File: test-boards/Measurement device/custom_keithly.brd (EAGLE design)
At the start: 160 x 100 mm, 49 parts, among them IC1 TL071D, IC2 7805L, IC3 7905L, U1 AD8220, U2 INA333, U3 INA333

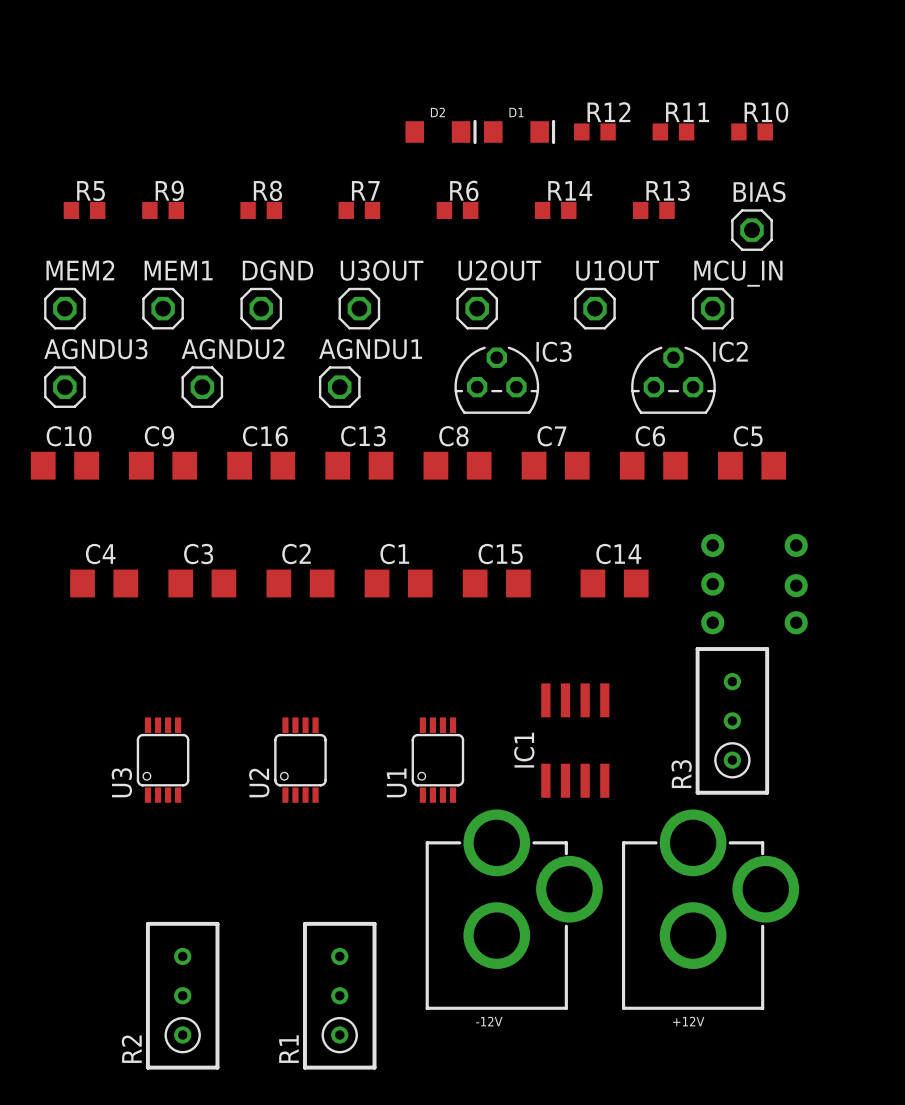
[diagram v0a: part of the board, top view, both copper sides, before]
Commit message: added doc for required .lbr files and basic BOM
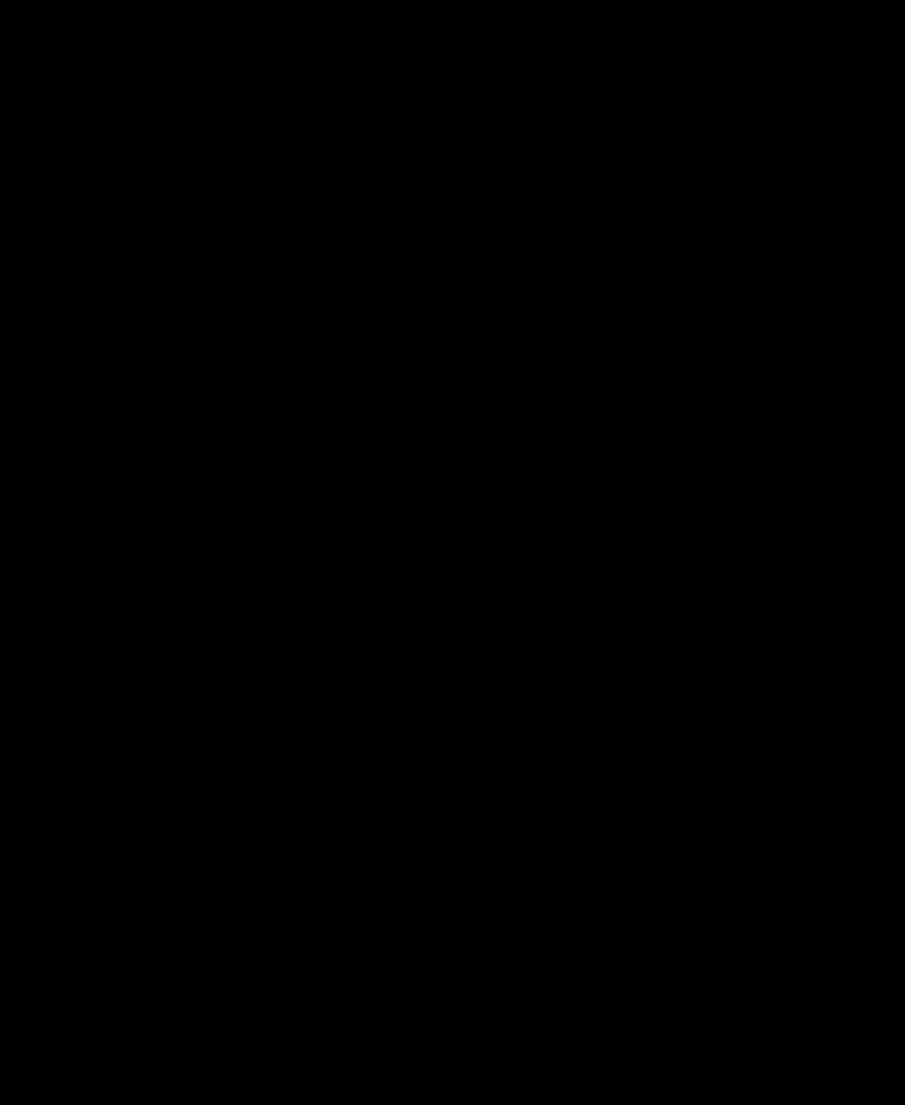
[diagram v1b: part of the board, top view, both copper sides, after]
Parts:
- removed +12V, -12V: POWER_JACK, SparkFun-Connectors:POWER_JACK_PTH
- removed AGNDU1, AGNDU2, AGNDU3, BIAS, DGND, MCU_IN, MEM1, MEM2, U1OUT, U2OUT, U3OUT: (no value), pinhead:1X01
- removed C1, C13, C16, C2, C3, C4, C5, C6, C7, C8: 0.1uF, rcl:C3216
- removed C10, C9: 10uF, rcl:C3216
- removed C14, C15: 0.33uF, rcl:C3216
- removed D1: RED, SparkFun-LED:LED-1206
- removed D2: YELLOW, SparkFun-LED:LED-1206
- removed IC1: TL071D, linear:SO08
- removed IC2: 7805L, linear:TO92
- removed IC3: 7905L, linear:TO92
- removed R1, R2, R3: 100R, rcl:RTRIM3296W
- removed R10, R11, R12: 30R, rcl:R0603
- removed R13, R14: 220R, rcl:R0603
- removed R5: 10R, rcl:R0603
- removed R6, R7, R8, R9: 100K, rcl:R0603
- removed U$1: PS850L_BUTTON, untitled:PS850L
- removed U1: AD8220, untitled:MSOP08
- removed U2, U3: INA333, untitled:MSOP08
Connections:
- removed net +5V: C1.1, C3.1, C5.1, C7.1, C9.1, D1.C, IC1.7, U$1.P$6, U1.8, U2.7, U3.7
- removed net -5V: C10.1, C2.2, C4.2, C6.2, C8.1, D2.A, IC1.4, U$1.P$3, U1.5, U2.4, U3.4
- removed net AGND: +12V.GNDBREAK, -12V.GNDBREAK, AGNDU1.1, AGNDU2.1, AGNDU3.1, C1.2, C10.2, C2.1, C3.2, C4.1, C5.2, C6.1, C7.2, C8.2, C9.2, MEM2.1, U1.6, U2.3, U2.5, U3.3, U3.5
- removed net GND: +12V.GND, -12V.GND, C13.1, C14.1, C15.2, C16.2, DGND.1, IC2.2, IC3.1, R13.1, R14.1, R9.2
- removed net IN+: IC1.6, R5.1, R7.2, U1.4
- removed net IN-: MEM1.1, R5.2, U1.1
- removed net MCU_IN: MCU_IN.1, R8.1
- removed net N$1: IC1.2, R6.2, R7.1
- removed net N$10: -12V.PWR, C15.1, IC3.2
- removed net N$11: C13.2, IC2.1, U$1.P$5
- removed net N$15: C16.1, IC3.3, U$1.P$2
- removed net N$2: IC1.3, R8.2, R9.1
- removed net N$3: R1.1, R10.1
- removed net N$4: R11.1, R2.3
- removed net N$5: R12.1, R3.3
- removed net N$7: +12V.PWR, C14.2, IC2.3
- removed net N$8: D1.A, R13.2
- removed net N$9: D2.C, R14.2
- removed net U1OUT: U1.7, U1OUT.1, U2.2
- removed net U1RG1: R1.2, U1.3
- removed net U1RG2: R10.2, U1.2
- removed net U2OUT: U2.6, U2OUT.1, U3.2
- removed net U2RG1: R11.2, U2.1
- removed net U2RG2: R2.2, U2.8
- removed net U3OUT: U3.6, U3OUT.1
- removed net U3RG1: R12.2, U3.1
- removed net U3RG2: R3.2, U3.8
- removed net V+: BIAS.1, R6.1

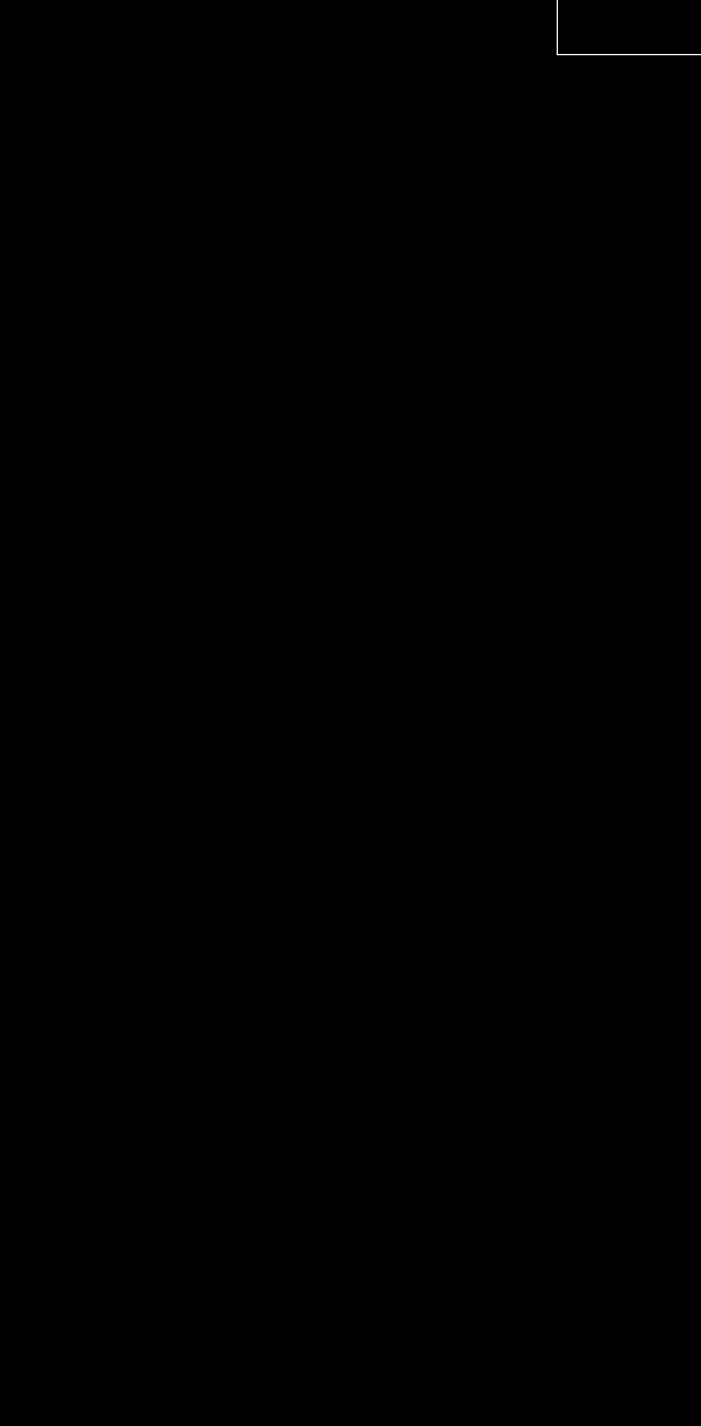
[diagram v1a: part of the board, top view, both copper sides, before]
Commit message: created part of the schematic and added some datasheets
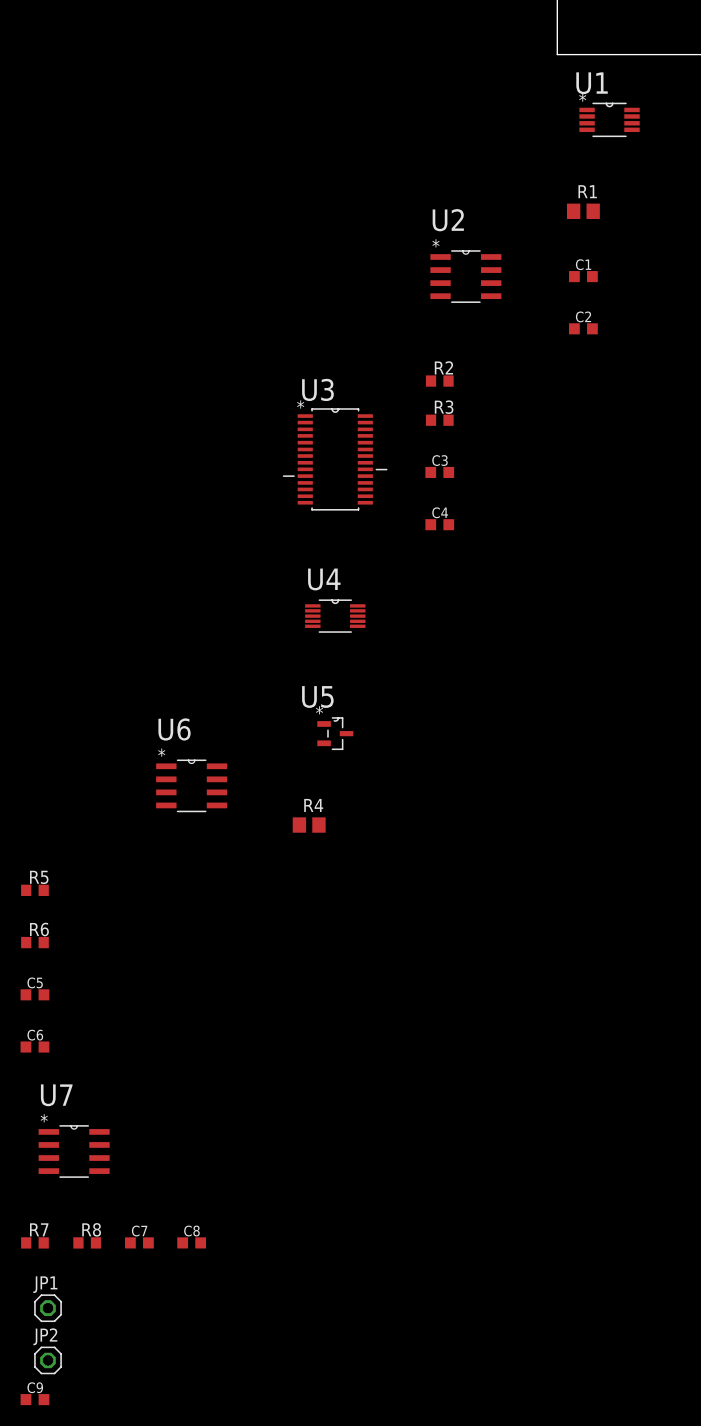
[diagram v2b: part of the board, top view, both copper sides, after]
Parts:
- added C1, C2, C3, C4, C5, C6, C7, C8, C9: 0.1u, resistor:C0603K
- added JP1, JP2: (no value), pinhead:1X01
- added R1: 80.6, resistor:R0805
- added R2, R3, R5, R6, R7, R8: 20K, resistor:R0603
- added R4: 300, resistor:R0805
- added U1: AD8227BRMZ, Analog Devices_By_element14_Batch_1:SOP65P490X110-8N
- added U2, U6, U7: AD820ARZ-REEL7, ADI-Phase-2:SOIC127P600X175-8N
- added U3: ADS1248IPWR, Texas Instruments_By_element14_Batch_1:SOP65P640X120-28N
- added U4: AD5302BRMZ-REEL7, ADI-Phase-2:SOP50P490X110-10N
- added U5: LM4040A20IDBZT, Texas Instruments_By_element14_Batch_1:SOT95P237X112-3N
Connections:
- new net +5V: C1.2, C3.2, C5.2, C7.2, R4.1, U1.8, U2.7, U4.2, U6.7, U7.7
- new net -5V: C2.2, C4.2, C6.2, C8.2, U1.5, U2.4, U6.4, U7.4
- new net 2.048V: C9.2, R4.2, R6.2, R8.2, U4.3, U4.4, U5.1
- new net AGND: C1.1, C2.1, C3.1, C4.1, C5.1, C6.1, C7.1, C8.1, C9.1, U4.10, U5.2
- new net AVDD: U3.22
- new net AVSS: U3.21
- new net DACA: JP1.1, R5.1, U6.6
- new net DACB: R7.1, U2.3, U7.6
- new net DAC_VOUTA: U4.5, U6.3
- new net DAC_VOUTB: U4.6, U7.3
- new net DVDD: U3.1
- new net IN+: U1.1
- new net IN-: U1.4
- new net N$1: R1.2, U1.2
- new net N$2: R1.1, U1.3
- new net N$3: R2.1, R3.2, U2.2
- new net N$5: R5.2, R6.1, U6.2
- new net N$7: R7.2, R8.1, U7.2
- new net VOUTN: R3.1, U1.6, U2.6
- new net VOUTP: R2.2, U1.7

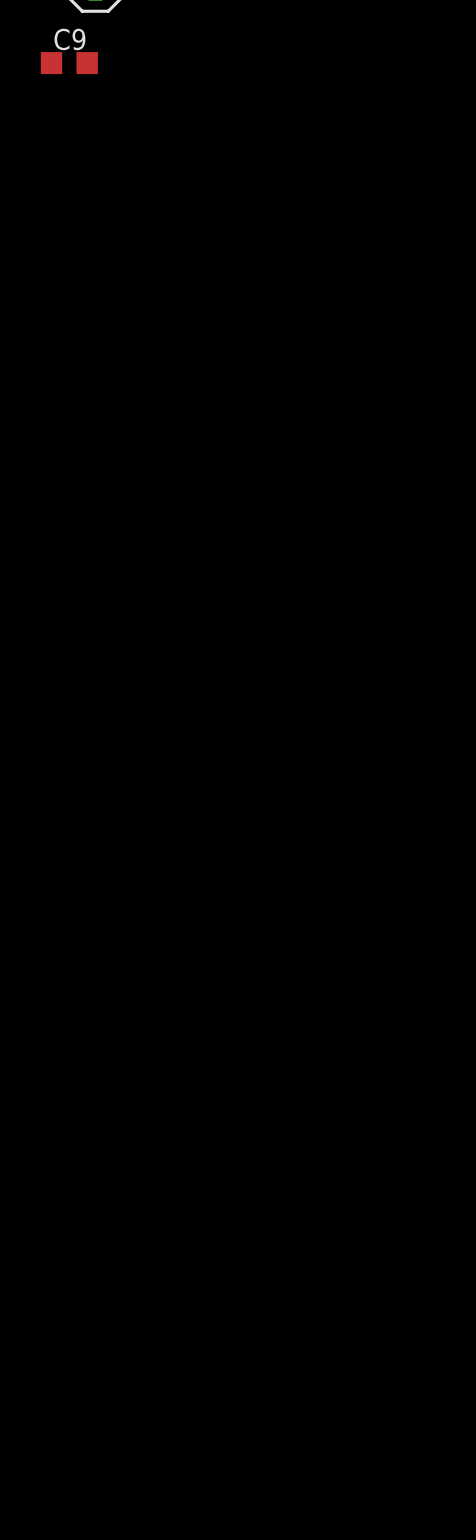
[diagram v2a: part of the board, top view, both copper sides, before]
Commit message: Analog part of schematic complete
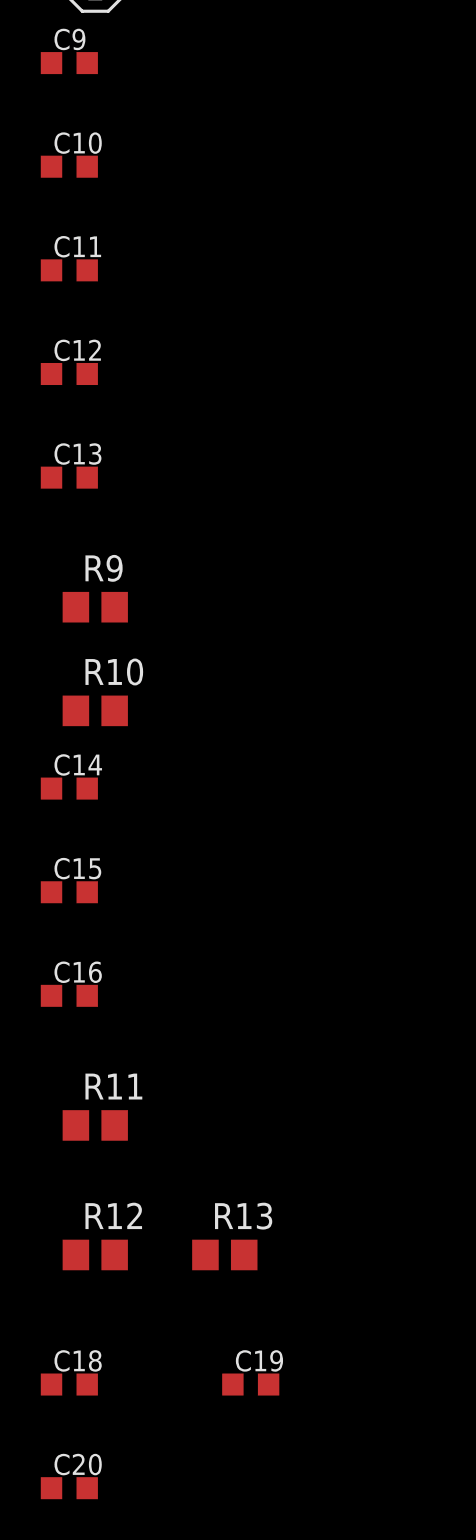
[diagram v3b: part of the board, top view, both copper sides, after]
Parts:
- added C10: 47u, resistor:C0603K
- added C11, C12, C13: 0.1u, resistor:C0603K
- added C14, C18: 100n, resistor:C0603K
- added C15, C16, C19, C20: 10n, resistor:C0603K
- added R10, R12, R13, R9: 1K, resistor:R0805
- added R11: 10R, resistor:R0805
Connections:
- removed net AVDD: U3.22
- removed net AVSS: U3.21
- removed net DVDD: U3.1
- new net +3V3: C11.2, U3.1
- new net GND: C11.1, U3.2
- new net N$11: JP2.1, R11.2, R13.1
- new net N$4: C10.2, U3.9
- new net N$6: C10.1, U3.10
- new net N$8: C14.1, C15.2, R9.2, U3.12
- new net N$9: C14.2, C16.1, R10.2, U3.11
- net +5V: now also C12.2, U3.22
- net -5V: now also C13.2, U3.21
- net AGND: now also C12.1, C13.1, C15.1, C16.2, C19.1, C20.2, R11.1, R12.1
- net IN+: now also C18.2, C20.1, R13.2
- net IN-: now also C18.1, C19.2, R12.2
- net VOUTN: now also R9.1
- net VOUTP: now also R10.1

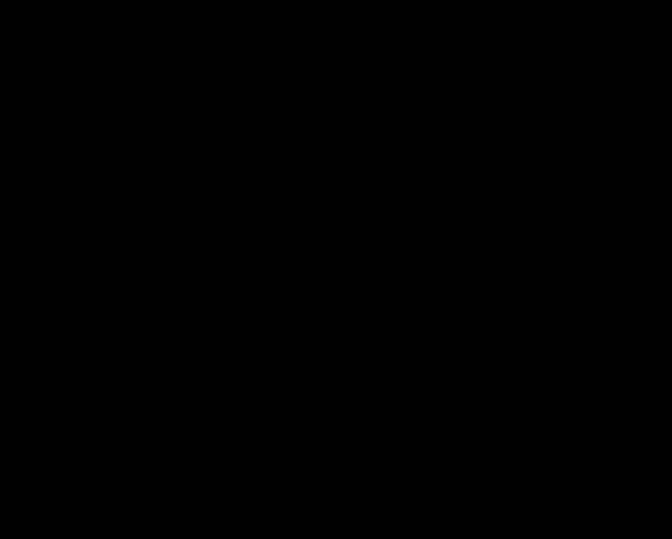
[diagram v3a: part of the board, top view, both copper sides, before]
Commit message: added unconnected controlller
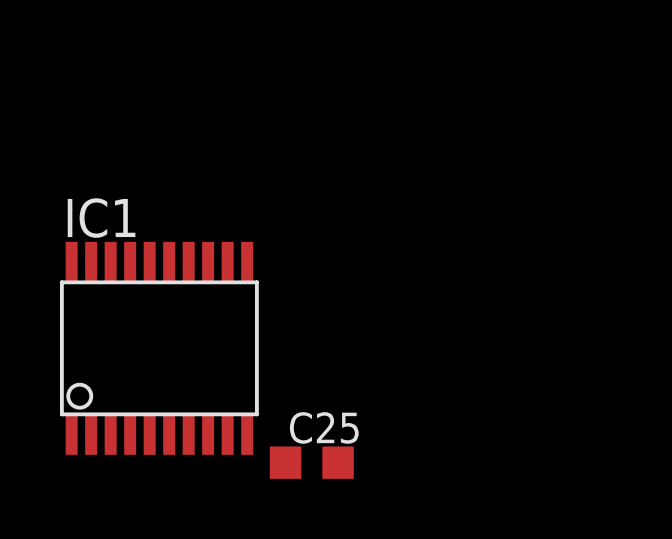
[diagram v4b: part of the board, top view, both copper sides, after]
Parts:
- added C25: 0.1u, resistor:C0603K
- added IC1: STM32F030F4P, micro-stm_v3:TSSOP20-I
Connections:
- new net VDDA: IC1.5
- new net VSS: IC1.15
- net +3V3: now also IC1.16
- net +5V: now also C25.2
- net AGND: now also C25.1, U3.13, U3.14, U3.15, U3.16, U3.17, U3.18
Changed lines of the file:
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@@
 <attribute name="VALUE" x="-51.6" y="-202.31" size="1.016" layer="27"/>
+</element>
+<element name="C25" library="resistor" library_urn="urn:adsk.eagle:library:348" package="C0603K" package3d_urn="urn:adsk.eagle:package:23680/2" value="0.1u" x="-50.8" y="-254" smashed="yes">
+<attribute name="NAME" x="-51.6" y="-253.35" size="1.016" layer="25"/>
+<attribute name="VALUE" x="-51.6" y="-255.65" size="1.016" layer="27"/>
+</element>
+<element name="IC1" library="micro-stm_v3" package="TSSOP20-I" value="STM32F030F4P" x="-55.88" y="-250.19" smashed="yes">
+<attribute name="NAME" x="-59.09" y="-246.48" size="1.27" layer="25"/>
+<attribute name="VALUE" x="-59.13" y="-255.085" size="1.27" layer="27"/>
 </element>
 </elements>
@@
 <contactref element="U2" pad="7"/>
 <contactref element="C3" pad="2"/>
-<contactref element="U4" pad="2"/>
 <contactref element="R4" pad="1"/>
 <contactref element="C5" pad="2"/>
@@
 <contactref element="C12" pad="2"/>
 <contactref element="U3" pad="22"/>
+<contactref element="U4" pad="2"/>
+<contactref element="C25" pad="2"/>
 <wire x1="-39.765" y1="-115.57" x2="-49.925" y2="-146.05" width="0" layer="19" extent="1-1"/>
 <wire x1="-44.5262" y1="-106.045" x2="-39.765" y2="-115.57" width="0" layer="19" extent="1-1"/>
@@
 <wire x1="3.415" y1="-21.59" x2="-6.4262" y2="-20.955" width="0" layer="19" extent="1-1"/>
 <wire x1="7.2644" y1="-5.3848" x2="3.415" y2="-21.59" width="0" layer="19" extent="1-1"/>
+<wire x1="-49.925" y1="-254" x2="-49.925" y2="-146.05" width="0" layer="19" extent="1-1"/>
 </signal>
 <signal name="IN+">
@@
 <contactref element="R11" pad="1"/>
 <contactref element="R12" pad="1"/>
+<contactref element="U3" pad="16"/>
+<contactref element="U3" pad="17"/>
+<contactref element="U3" pad="18"/>
+<contactref element="U3" pad="13"/>
+<contactref element="U3" pad="14"/>
+<contactref element="U3" pad="15"/>
+<contactref element="C25" pad="1"/>
 <wire x1="-42.785" y1="-195.58" x2="-49.925" y2="-200.66" width="0" layer="19" extent="1-1"/>
 <wire x1="-50.48" y1="-189.23" x2="-42.785" y2="-195.58" width="0" layer="19" extent="1-1"/>
@@
 <wire x1="-22.6822" y1="-66.9798" x2="-51.675" y2="-91.44" width="0" layer="19" extent="1-1"/>
 <wire x1="-19.4056" y1="-53.6194" x2="-22.6822" y2="-66.9798" width="0" layer="19" extent="1-1"/>
-<wire x1="-12.305" y1="-45.72" x2="-19.4056" y2="-53.6194" width="0" layer="19" extent="1-1"/>
-<wire x1="-12.305" y1="-40.64" x2="-12.305" y2="-45.72" width="0" layer="19" extent="1-1"/>
+<wire x1="-18.669" y1="-43.5864" x2="-19.4056" y2="-53.6194" width="0" layer="19" extent="1-1"/>
+<wire x1="-18.669" y1="-42.9514" x2="-18.669" y2="-43.5864" width="0" layer="19" extent="1-1"/>
+<wire x1="-18.669" y1="-42.291" x2="-18.669" y2="-42.9514" width="0" layer="19" extent="1-1"/>
+<wire x1="-18.669" y1="-41.656" x2="-18.669" y2="-42.291" width="0" layer="19" extent="1-1"/>
+<wire x1="-24.511" y1="-43.5864" x2="-18.669" y2="-43.5864" width="0" layer="19" extent="1-1"/>
+<wire x1="-24.511" y1="-42.9514" x2="-24.511" y2="-43.5864" width="0" layer="19" extent="1-1"/>
+<wire x1="-12.305" y1="-40.64" x2="-18.669" y2="-41.656" width="0" layer="19" extent="1-1"/>
+<wire x1="-12.305" y1="-45.72" x2="-12.305" y2="-40.64" width="0" layer="19" extent="1-1"/>
 <wire x1="1.665" y1="-26.67" x2="-12.305" y2="-40.64" width="0" layer="19" extent="1-1"/>
 <wire x1="1.665" y1="-21.59" x2="1.665" y2="-26.67" width="0" layer="19" extent="1-1"/>
+<wire x1="-51.675" y1="-254" x2="-49.925" y2="-200.66" width="0" layer="19" extent="1-1"/>
 </signal>
 <signal name="-5V">
@@
 <contactref element="C11" pad="2"/>
 <contactref element="U3" pad="1"/>
+<contactref element="IC1" pad="16"/>
+<wire x1="-56.205" y1="-247.315" x2="-49.925" y2="-140.97" width="0" layer="19" extent="1-1"/>
 <wire x1="-24.511" y1="-35.1536" x2="-49.925" y2="-140.97" width="0" layer="19" extent="1-1"/>
 </signal>
@@
 <wire x1="-49.53" y1="-127" x2="-48.58" y2="-182.88" width="0" layer="19" extent="1-1"/>
 </signal>
+<signal name="VDDA">
+<contactref element="IC1" pad="5"/>
+</signal>
+<signal name="VSS">
+<contactref element="IC1" pad="15"/>
+</signal>
 </signals>
